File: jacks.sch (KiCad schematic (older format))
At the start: 73 parts, among them J1 PJ301CM, J10 PJ301BM, J11 PJ301BM, J12 PJ301BM, J13 PJ301BM, J14 PJ301BM, J15 PJ301BM, J16 PJ301BM, J17 PJ301BM, J18 PJ301BM, J19 PJ301BM, J2 PJ301CM, J20 PJ301BM, J21 PJ301BM, J22 PJ301BM, J23 PJ301BM, J24 PJ301BM, J25 PJ301BM, J26 PJ301BM, J3 PJ301BM, J4 PJ301BM, J5 PJ301BM, J6 PJ301BM, J7 PJ301BM, J8 PJ301BM, J9 PJ301BM, Q1 MMBT3904, Q2 MMBT3904, Q3 MMBT3904, Q4 MMBT3904, U1 VO0600T, U2 74LV1T34, U6 MCP6004

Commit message: Added JCLC part numbers.
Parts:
- C10, C21, C7, C9: symbol Device:C -> sequencer-rescue:C-Device
- C22: symbol Device:C -> sequencer-rescue:C-Device; LCSC (none) -> C1588
- D2: symbol Device:D -> sequencer-rescue:D-Device
- Q1, Q2, Q3, Q4: symbol Transistor_BJT:MMBT3904 -> sequencer-rescue:MMBT3904-Transistor_BJT
- R1: symbol Device:R -> sequencer-rescue:R-Device; LCSC (none) -> C22962
- R14, R15, R16, R17, R18, R19, R2, R20, R21, R26, R27, R3, R30, R31, R32, R33, R37, R38, R39, R4, R45, R46, R6, R68, R7, R78, R80, R81, R83, R84, R85, R86: symbol Device:R -> sequencer-rescue:R-Device
- R40: symbol Device:R -> sequencer-rescue:R-Device; LCSC (none) -> C25811
- U2: LCSC (none) -> C100024
- U6: symbol Amplifier_Operational:MCP6004 -> sequencer-rescue:MCP6004-Amplifier_Operational; LCSC (none) -> C7378
- U6: symbol Amplifier_Operational:MCP6004 -> sequencer-rescue:MCP6004-Amplifier_Operational

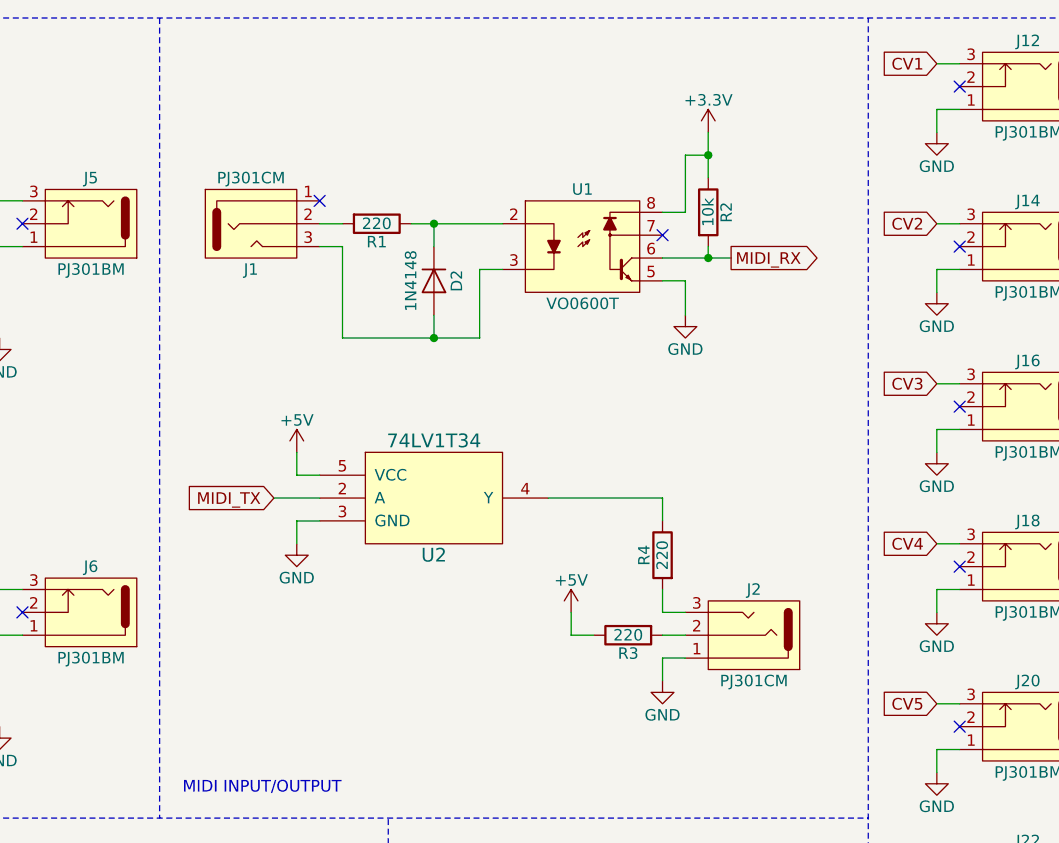
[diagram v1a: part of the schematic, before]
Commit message: Added solder jumpers for midi polarity and midi out/through.
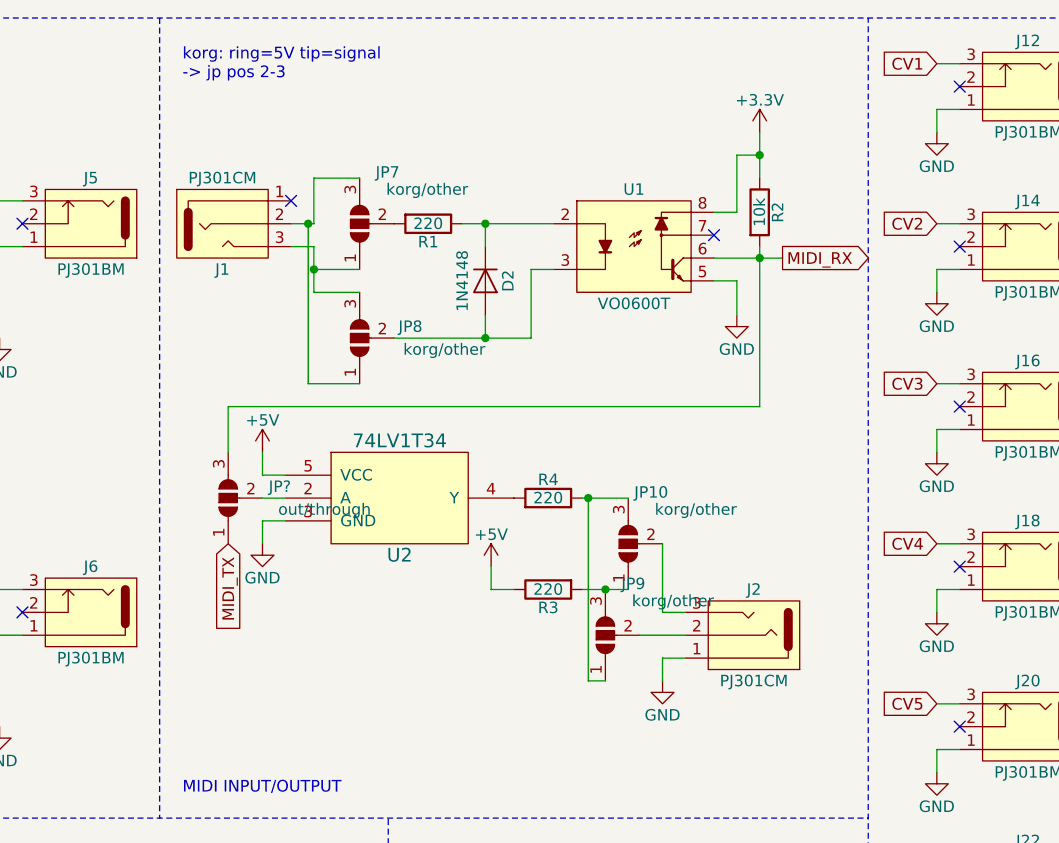
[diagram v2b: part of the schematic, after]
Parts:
- added JP10, JP7, JP8, JP9: korg/other, Jumper:SolderJumper-3_P1.3mm_Open_Pad1.0x1.5mm, symbol Jumper:SolderJumper_3_Open
- added JP?: out/through, Jumper:SolderJumper-3_P1.3mm_Open_Pad1.0x1.5mm, symbol Jumper:SolderJumper_3_Open
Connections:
- net MIDI_RX: now also JP?.3 (B)
- net MIDI_TX: now also JP?.1 (A); no longer U2.2 (A)
- net at J1.2: now also JP7.3 (B), JP8.1 (A); no longer R1.2
- net at D2.2 (A), U1.3: now also JP8.2 (C); no longer J1.3
- net at J2.2: now also JP9.2 (C); no longer R3.2
- net at J2.3: now also JP10.2 (C); no longer R4.2
- net at R4.1: now also JP10.3 (B), JP9.1 (A); no longer U2.4 (Y)
- new net: J1.3, JP7.1 (A), JP8.3 (B)
- new net: JP10.1 (A), JP9.3 (B), R3.2
- new net: JP7.2 (C), R1.2
- new net: R4.2, U2.4 (Y)
- new net: JP?.2 (C), U2.2 (A)
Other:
- note added: "korg: ring=5V tip=signal\n-> jp pos 2-3"
- moved on the sheet: D2, J1, R1, R2, R3, R4, U1, U2

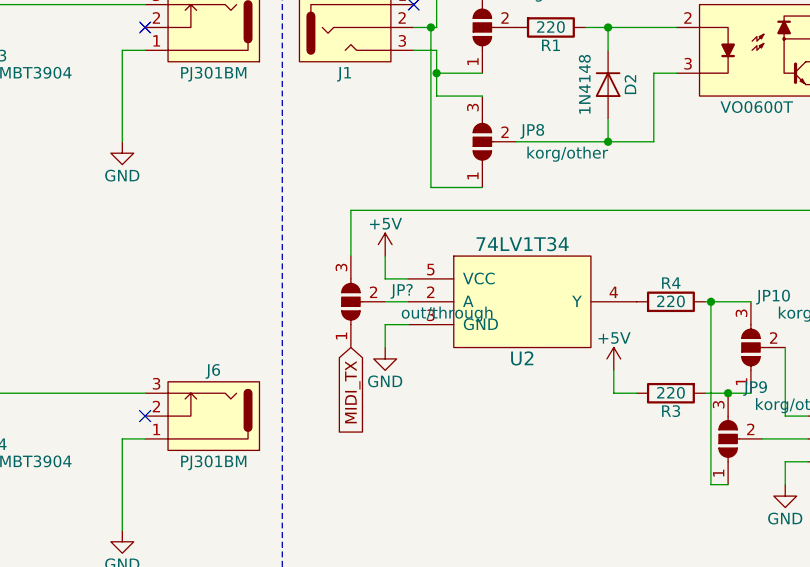
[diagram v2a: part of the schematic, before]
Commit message: Some cleanup. Frontpanel with Copper Labels.
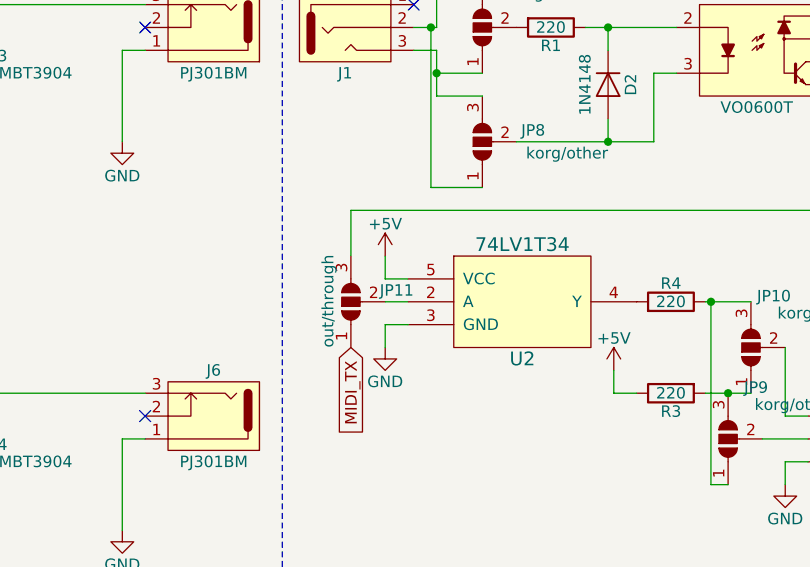
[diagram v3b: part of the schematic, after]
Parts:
- gave numbers to parts that had none: 1
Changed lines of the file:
@@
 korg: ring=5V tip=signal\n-> jp pos 2-3
 $Comp
-L Jumper:SolderJumper_3_Open JP?
+L Jumper:SolderJumper_3_Open JP11
 U 1 1 5F1CCD60
 P 5700 2700
-F 0 "JP?" V 5750 2425 50  0000 L CNN
-F 1 "out/through" V 5650 2075 50  0000 L CNN
+F 0 "JP11" V 5750 2425 50  0000 L CNN
+F 1 "out/through" H 5500 2800 50  0000 L CNN
 F 2 "Jumper:SolderJumper-3_P1.3mm_Open_Pad1.0x1.5mm" H 5700 2700 50  0001 C CNN
 F 3 "~" H 5700 2700 50  0001 C CNN
